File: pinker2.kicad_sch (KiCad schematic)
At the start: 30 parts, among them J1 XLR3, Q1 BC549C, U1 OPA2134

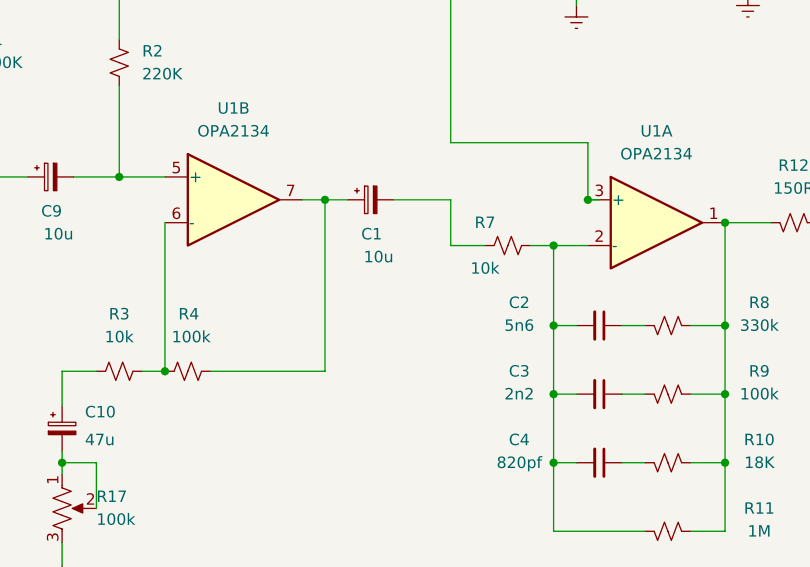
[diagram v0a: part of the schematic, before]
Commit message: layout progress
started adding traces
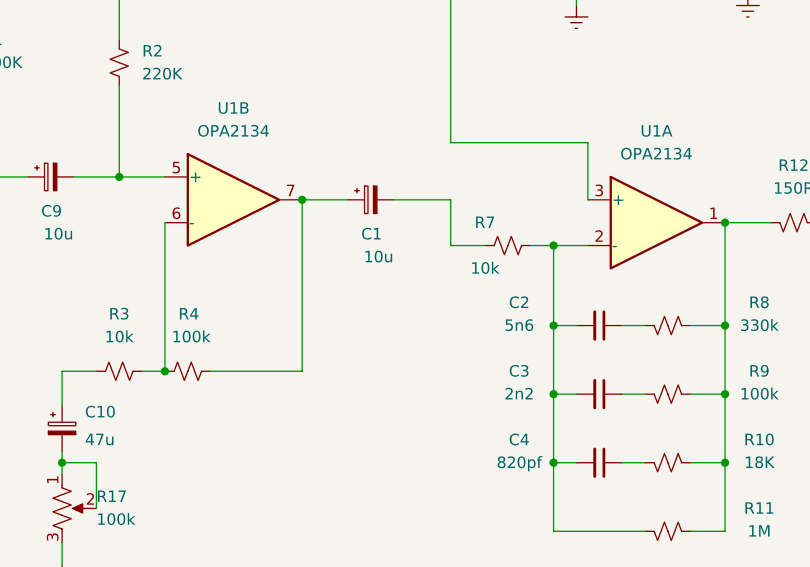
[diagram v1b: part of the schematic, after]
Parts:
- C10: footprint Capacitor_THT:CP_Radial_D6.3mm_P2.50mm -> Capacitor_THT:CP_Radial_D4.0mm_P1.50mm
- C2, C3, C4, C7: footprint Capacitor_THT:CP_Radial_D4.0mm_P1.50mm -> Capacitor_THT:C_Disc_D3.0mm_W1.6mm_P2.50mm
- R1, R10, R11, R12, R13, R14, R15, R2, R3, R4, R5, R6, R7, R8, R9: footprint Resistor_THT:R_Axial_DIN0207_L6.3mm_D2.5mm_P5.08mm_Vertical -> Resistor_THT:R_Axial_DIN0204_L3.6mm_D1.6mm_P1.90mm_Vertical
- R17: footprint Resistor_THT:R_Axial_DIN0207_L6.3mm_D2.5mm_P5.08mm_Vertical -> Potentiometer_THT:Potentiometer_Bourns_3266X_Horizontal
- U1: footprint Package_SO:SOIC-8-1EP_3.9x4.9mm_P1.27mm_EP2.41x3.81mm -> Package_DIP:DIP-8_W7.62mm_Socket

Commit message: almost complete
nudged some items, added a ground pour, linked the footprints to a local library (hopefully symbols live there too) added a pdf of the layout to help with visual diffs
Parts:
- C1, C10, C9: footprint Capacitor_THT:CP_Radial_D4.0mm_P1.50mm -> Library:CP_Radial_D4.0mm_P1.50mm
- C11, C5, C6, C8: footprint Capacitor_THT:CP_Radial_D10.0mm_P5.00mm -> Library:CP_Radial_D10.0mm_P5.00mm
- C2, C3, C4, C7: footprint Capacitor_THT:C_Disc_D3.0mm_W1.6mm_P2.50mm -> Library:C_Disc_D3.0mm_W1.6mm_P2.50mm
- J1: footprint Connector_Audio:Jack_XLR_Neutrik_NC3MBH_Horizontal -> Library:Jack_XLR_Neutrik_NC3MBH_Horizontal
- Q1: footprint Package_TO_SOT_THT:TO-92_Inline -> Library:TO-92_Inline
- R1, R10, R11, R12, R13, R14, R15, R2, R3, R4, R5, R6, R7, R8, R9: footprint Resistor_THT:R_Axial_DIN0204_L3.6mm_D1.6mm_P1.90mm_Vertical -> Library:R_Axial_DIN0204_L3.6mm_D1.6mm_P1.90mm_Vertical
- R17: footprint Potentiometer_THT:Potentiometer_Bourns_3266X_Horizontal -> Library:Potentiometer_Bourns_3266X_Horizontal
- U1: footprint Package_DIP:DIP-8_W7.62mm_Socket -> Library:DIP-8_W7.62mm_Socket
